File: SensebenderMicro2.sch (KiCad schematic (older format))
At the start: 40 parts, among them P2 MYSX_2.4, P3 Antenna, U1 ATSAMD21E, U2 MCP1703T-3302E, U3 NRF24L01, U4 RFM69HW, U5 ATSHA204A, U6 AT45DB041E, U7 Si7021, U8 AT24C32-STUM-T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

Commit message: Updates to layout, copper pour etc
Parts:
- removed D2: LED, LEDs:LED-0603, symbol LED
- removed R3: 220R, Resistors_SMD:R_0603, symbol R
- D1, D3: symbol LED -> LED-RESCUE-SensebenderMicro2
- P3: footprint Pin_Headers:Pin_Header_Straight_1x01 -> Pin_Headers:Pin_Header_Angled_1x02
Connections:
- wire segments 62 -> 60
- no-connect marks 6 -> 7
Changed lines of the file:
@@
 LIBS:mysensors_mcu
 LIBS:SensebenderMicro2-cache
-EELAYER 25 0
+EELAYER 26 0
 EELAYER END
 $Descr A4 11693 8268
@@
 F 0 "P3" H 7800 1050 50  0000 C CNN
 F 1 "Antenna" V 7900 950 50  0000 C CNN
-F 2 "Pin_Headers:Pin_Header_Straight_1x01" H 7800 950 50  0001 C CNN
+F 2 "Pin_Headers:Pin_Header_Angled_1x02" H 7800 950 50  0001 C CNN
 F 3 "" H 7800 950 50  0000 C CNN
 	1    7800 950
@@
 $EndComp
 $Comp
-L LED D2
-U 1 1 56B7B2DC
-P 5000 6600
-F 0 "D2" H 5000 6700 50  0000 C CNN
-F 1 "LED" H 5000 6500 50  0000 C CNN
-F 2 "LEDs:LED-0603" H 5000 6600 50  0001 C CNN
-F 3 "" H 5000 6600 50  0000 C CNN
-	1    5000 6600
-	0    -1   -1   0
-$EndComp
-$Comp
-L LED D1
+L LED-RESCUE-SensebenderMicro2 D1
 U 1 1 56B7B443
 P 4700 6600
@@
 $EndComp
 $Comp
-L R R3
-U 1 1 56B7B574
-P 5000 6250
-F 0 "R3" V 5080 6250 50  0000 C CNN
-F 1 "220R" V 5000 6250 50  0000 C CNN
-F 2 "Resistors_SMD:R_0603" V 4930 6250 50  0001 C CNN
-F 3 "" H 5000 6250 50  0000 C CNN
-	1    5000 6250
-	1    0    0    -1
-$EndComp
-$Comp
 L GND #PWR014
 U 1 1 56B7B5F3
@@
 $EndComp
 $Comp
-L GND #PWR015
-U 1 1 56B7B627
-P 5000 6800
-F 0 "#PWR015" H 5000 6550 50  0001 C CNN
-F 1 "GND" H 5000 6650 50  0000 C CNN
-F 2 "" H 5000 6800 50  0000 C CNN
-F 3 "" H 5000 6800 50  0000 C CNN
-	1    5000 6800
-	1    0    0    -1
-$EndComp
-$Comp
 L ATSHA204A U5
 U 1 1 56B7BA20
@@
 	1    0    0    -1
 $EndComp
-Text Label 3600 4850 0    60   ~ 0
+Text Label 3600 5850 0    60   ~ 0
 FLS_CS
 $Comp
@@
 $EndComp
 $Comp
-L +3V3 #PWR034
+L +3V3 #PWR032
 U 1 1 5726438E
 P 8300 2900
-F 0 "#PWR034" H 8300 2750 50  0001 C CNN
+F 0 "#PWR032" H 8300 2750 50  0001 C CNN
 F 1 "+3V3" H 8315 3073 50  0000 C CNN
 F 2 "" H 8300 2900 50  0000 C CNN
@@
 Wire Wire Line
 	4700 5950 4700 6100
-Wire Wire Line
-	5000 5850 5000 6100
 Wire Wire Line
 	5250 1300 5250 1650
@@
 Connection ~ 10000 1050
 $Comp
-L GND #PWR035
+L GND #PWR033
 U 1 1 5761A76F
 P 9600 1100
-F 0 "#PWR035" H 9600 850 50  0001 C CNN
+F 0 "#PWR033" H 9600 850 50  0001 C CNN
 F 1 "GND" H 9605 927 50  0000 C CNN
 F 2 "" H 9600 1100 50  0000 C CNN
@@
 LEGACY_ID
 $Comp
-L +3.3VA #PWR036
+L +3.3VA #PWR034
 U 1 1 5828CA22
 P 2300 2900
-F 0 "#PWR036" H 2300 2750 50  0001 C CNN
+F 0 "#PWR034" H 2300 2750 50  0001 C CNN
 F 1 "+3.3VA" H 2315 3073 50  0000 C CNN
 F 2 "" H 2300 2900 50  0000 C CNN
@@
 Wire Wire Line
 	4400 5050 4400 4950
-Wire Wire Line
-	3600 5850 5000 5850
 Wire Wire Line
 	3600 5950 4700 5950
@@
 $EndComp
 $Comp
-L +3V3 #PWR037
+L +3V3 #PWR035
 U 1 1 582A3CE8
 P 950 6650
-F 0 "#PWR037" H 950 6500 50  0001 C CNN
+F 0 "#PWR035" H 950 6500 50  0001 C CNN
 F 1 "+3V3" H 965 6823 50  0000 C CNN
 F 2 "" H 950 6650 50  0000 C CNN
@@
 $EndComp
 $Comp
-L +3V3 #PWR038
+L +3V3 #PWR036
 U 1 1 582F12E3
 P 10200 2900
-F 0 "#PWR038" H 10200 2750 50  0001 C CNN
+F 0 "#PWR036" H 10200 2750 50  0001 C CNN
 F 1 "+3V3" H 10215 3073 50  0000 C CNN
 F 2 "" H 10200 2900 50  0000 C CNN
@@
 D5_PWM
 $Comp
-L LED D3
+L LED-RESCUE-SensebenderMicro2 D3
 U 1 1 5838D210
 P 5300 6600
@@
 $EndComp
 $Comp
-L GND #PWR039
+L GND #PWR037
 U 1 1 5838D21C
 P 5300 6800
-F 0 "#PWR039" H 5300 6550 50  0001 C CNN
+F 0 "#PWR037" H 5300 6550 50  0001 C CNN
 F 1 "GND" H 5300 6650 50  0000 C CNN
 F 2 "" H 5300 6800 50  0000 C CNN
@@
 	5300 6050 5300 6100
 $Comp
-L +3.3V #PWR?
+L +3.3V #PWR038
 U 1 1 5838DA32
 P 8550 900
-F 0 "#PWR?" H 8550 750 50  0001 C CNN
+F 0 "#PWR038" H 8550 750 50  0001 C CNN
 F 1 "+3.3V" H 8565 1073 50  0000 C CNN
 F 2 "" H 8550 900 50  0000 C CNN
@@
 $EndComp
 $Comp
-L +3.3V #PWR?
+L +3.3V #PWR039
 U 1 1 5838DABF
 P 10000 1000
-F 0 "#PWR?" H 10000 850 50  0001 C CNN
+F 0 "#PWR039" H 10000 850 50  0001 C CNN
 F 1 "+3.3V" H 10015 1173 50  0000 C CNN
 F 2 "" H 10000 1000 50  0000 C CNN
@@
 $EndComp
 $Comp
-L GND #PWR?
+L GND #PWR040
 U 1 1 583B0428
 P 7850 1150
-F 0 "#PWR?" H 7850 900 50  0001 C CNN
+F 0 "#PWR040" H 7850 900 50  0001 C CNN
 F 1 "GND" V 7855 1022 50  0000 R CNN
 F 2 "" H 7850 1150 50  0000 C CNN
@@
 	0    -1   -1   0
 $EndComp
+NoConn ~ 3600 4850
 $EndSCHEMATC

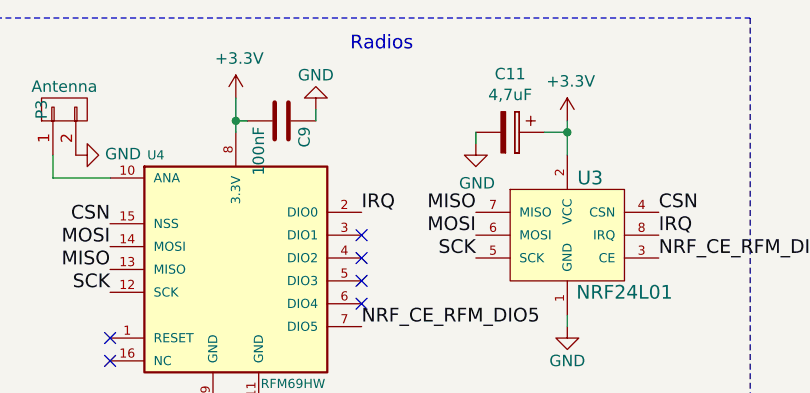
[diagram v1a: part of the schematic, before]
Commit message: Added extra 10uF caps to radios
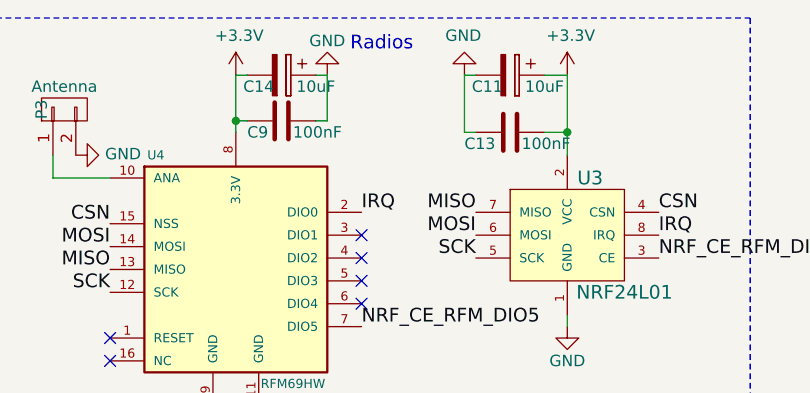
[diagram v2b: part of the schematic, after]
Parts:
- added C13: 100nF, Capacitors_SMD:C_0603, symbol C
- added C14: 10uF, Capacitors_SMD:C_0603, symbol CP
- C11: value 4,7uF -> 10uF
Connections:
- net +3V3: now also C13.1, C14.2
- net GND: now also C13.2, C14.1
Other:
- moved on the sheet: C11

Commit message: Updated vendor references
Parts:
- FB1: Vendor (none) -> Murata; Vendor part (none) -> BLM18PG471SN1D
- U1: value ATSAMD21E -> ATSAMD20E; Vendor (none) -> Atmel; Vendor part (none) -> ATSAMD20E18A-AN
- U2: Vendor (none) -> Microchip; Vendor part (none) -> MCP1703T-3302E/CB
- U5: Vendor (none) -> Micrhochip; Vendor part (none) -> ATSHA204A-STUCZ-T
- U6: Vendor (none) -> atmel; Vendor part (none) -> atmel
- U7: Vendor (none) -> Silicon; Vendor part (none) -> Si7041
- U8: value AT24C32-STUM-T -> 24AA32AT-I/OT; Vendor (none) -> Microchip; Vendor part (none) -> 24AA32AT-I/OT
- Y1: Vendor (none) -> Abracon; Vendor partno (none) -> ABS07-120-32.768kHz-T

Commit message: Changed to use RFM69HCW footprint (compatible with RFM95)
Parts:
- U4: symbol RFM69HW -> RFM95HW
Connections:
- net +3V3: now also U4.13 (3.3V); no longer U4.8 (3.3V)
- net CSN: now also U4.5 (NSS); no longer U4.15 (NSS)
- net GND: now also U4.1 (GND), U4.10 (GND), U4.8 (GND); no longer U4.11 (GND), U4.9 (GND)
- net IRQ: now also U4.14 (DIO0); no longer U4.2 (DIO0)
- net MISO: now also U4.2 (MISO); no longer U4.13 (MISO)
- net MOSI: now also U4.3 (MOSI); no longer U4.14 (MOSI)
- net SCK: now also U4.4 (SCK); no longer U4.12 (SCK)
- net ANT: now reaches P3.1 (P1)
- net ANT: now also U4.9 (ANA); no longer U4.10 (ANA)
- no-connect marks 7 -> 6
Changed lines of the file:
@@
 $EndComp
 $Comp
-L RFM69HW U4
+L RFM95HW U4
 U 1 1 55C1045B
 P 8550 1400
@@
 NoConn ~ 9100 1700
 NoConn ~ 9100 1800
-NoConn ~ 8000 2050
 $Comp
 L C C9
@@
 Wire Wire Line
 	9550 800  9550 1050
+Text Label 7800 1250 0    60   ~ 0
+ANT
 $EndSCHEMATC
